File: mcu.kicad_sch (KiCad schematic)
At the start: 11 parts, among them U5 ESP32-S3-WROOM-1

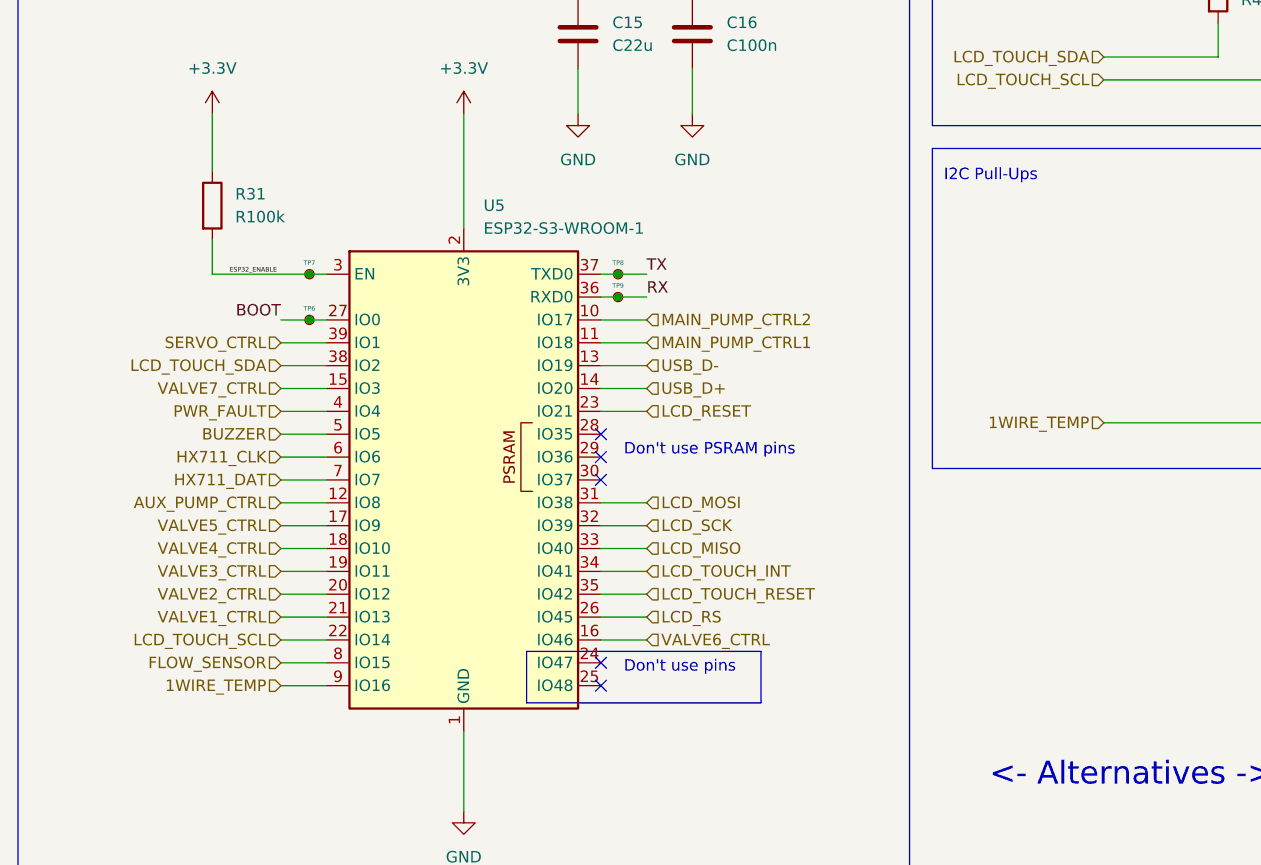
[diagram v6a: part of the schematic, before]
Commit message: Redesign power rails to use barrel jack 12V input
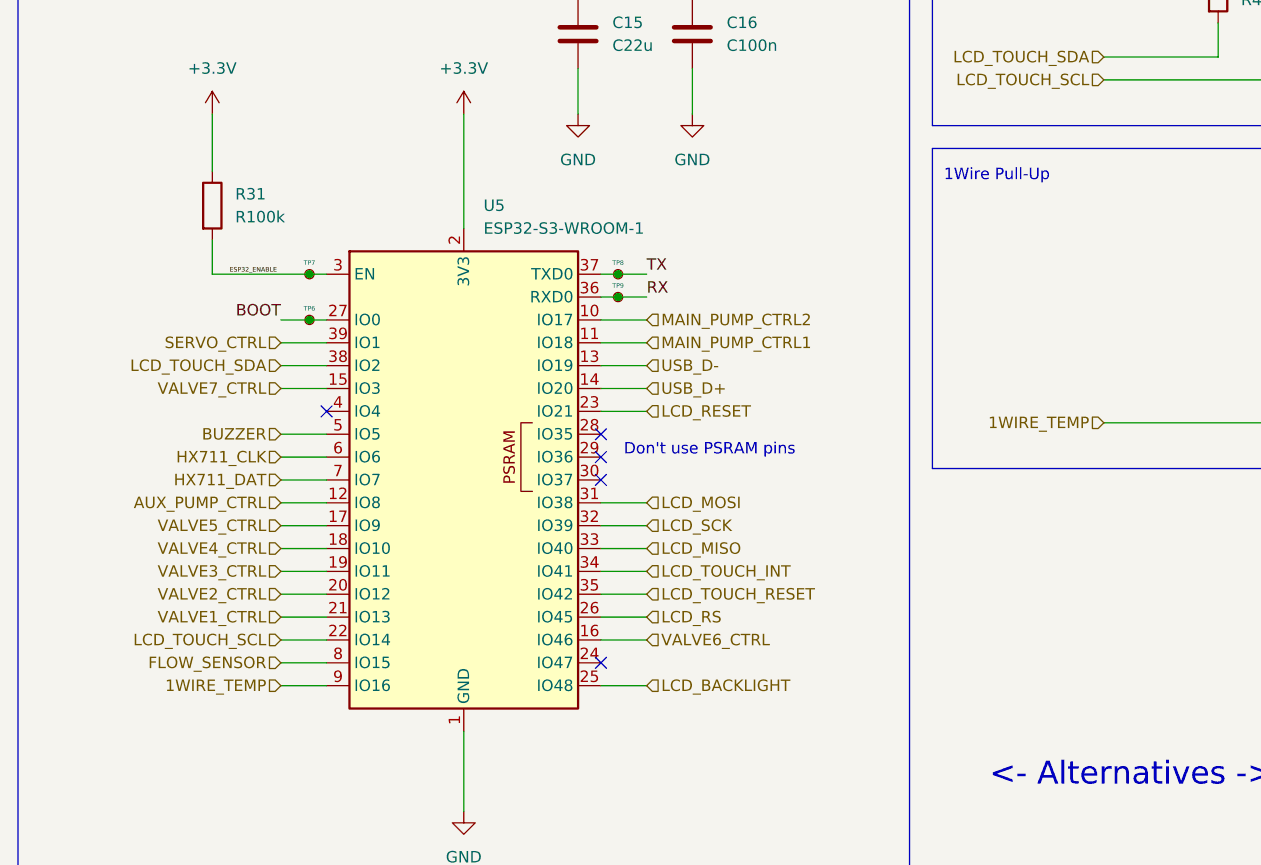
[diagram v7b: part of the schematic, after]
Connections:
- net LCD_BACKLIGHT: now reaches U5.25 (IO48)
- net PWR_FAULT: no longer names the net of U5.4 (IO4)
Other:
- note added: "1Wire Pull-Up"
- note removed: "Don't use pins"
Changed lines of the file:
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@@
   )
   (no_connect (at 78.74 125.73))
-  (no_connect (at 78.74 128.27))
+  (no_connect (at 48.26 97.79))
   (no_connect (at 78.74 105.41))
   (no_connect (at 78.74 102.87))
@@
     (stroke (width 0) (type default))
   )
-  (wire (pts (xy 43.18 97.79) (xy 48.26 97.79))
-    (stroke (width 0) (type default))
-  )
   (wire (pts (xy 43.18 123.19) (xy 48.26 123.19))
     (stroke (width 0) (type default))
@@
     (stroke (width 0) (type default))
   )
+  (wire (pts (xy 83.82 128.27) (xy 78.74 128.27))
+    (stroke (width 0) (type default))
+  )
   (wire (pts (xy 43.18 115.57) (xy 48.26 115.57))
     (stroke (width 0) (type default))
@@
   )
   (rectangle (start 115.57 68.58) (end 168.91 104.14)
-    (stroke (width 0) (type default))
-    (fill (type none))
-  )
-  (rectangle (start 70.485 124.46) (end 96.52 130.175)
     (stroke (width 0) (type default))
     (fill (type none))
@@
     (effects (font (size 2.54 2.54) (thickness 0.508) bold italic (color 255 69 42 1)) (justify left bottom))
   )
-  (text "Don't use pins" (at 81.28 127 0)
-    (effects (font (size 1.27 1.27)) (justify left bottom))
-  )
-  (text "I2C Pull-Ups" (at 116.84 72.39 0)
+  (text "1Wire Pull-Up" (at 116.84 72.39 0)
     (effects (font (size 1.27 1.27)) (justify left bottom))
   )
@@
     (effects (font (size 1.27 1.27)) (justify left))
   )
-  (hierarchical_label "PWR_FAULT" (shape input) (at 43.18 97.79 180) (fields_autoplaced)
-    (effects (font (size 1.27 1.27)) (justify right))
-  )
   (hierarchical_label "1WIRE_TEMP" (shape input) (at 43.18 128.27 180) (fields_autoplaced)
     (effects (font (size 1.27 1.27)) (justify right))
@@
     (effects (font (size 1.27 1.27)) (justify right))
   )
+  (hierarchical_label "LCD_BACKLIGHT" (shape input) (at 83.82 128.27 0) (fields_autoplaced)
+    (effects (font (size 1.27 1.27)) (justify left))
+  )
   (hierarchical_label "LCD_TOUCH_SCL" (shape input) (at 134.62 60.96 180) (fields_autoplaced)

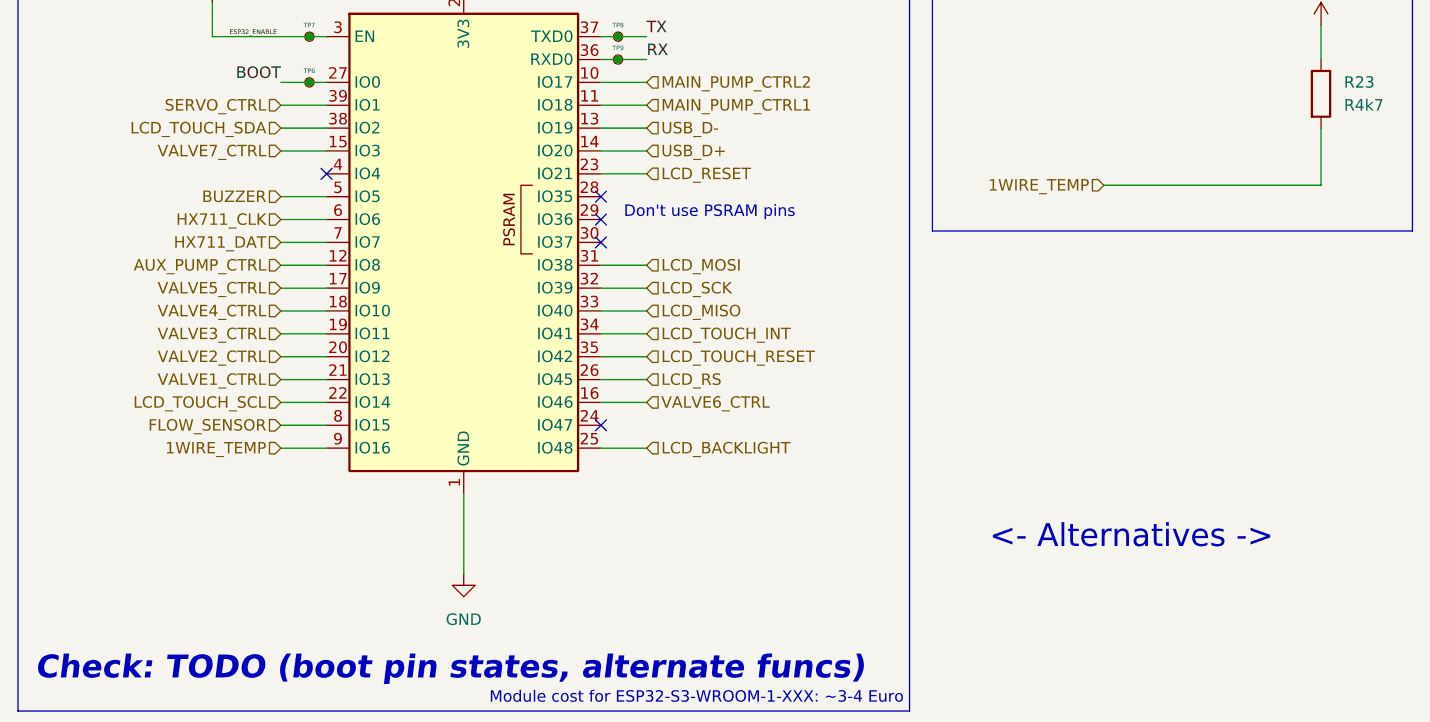
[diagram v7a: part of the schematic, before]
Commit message: Cleanup layout and schematic
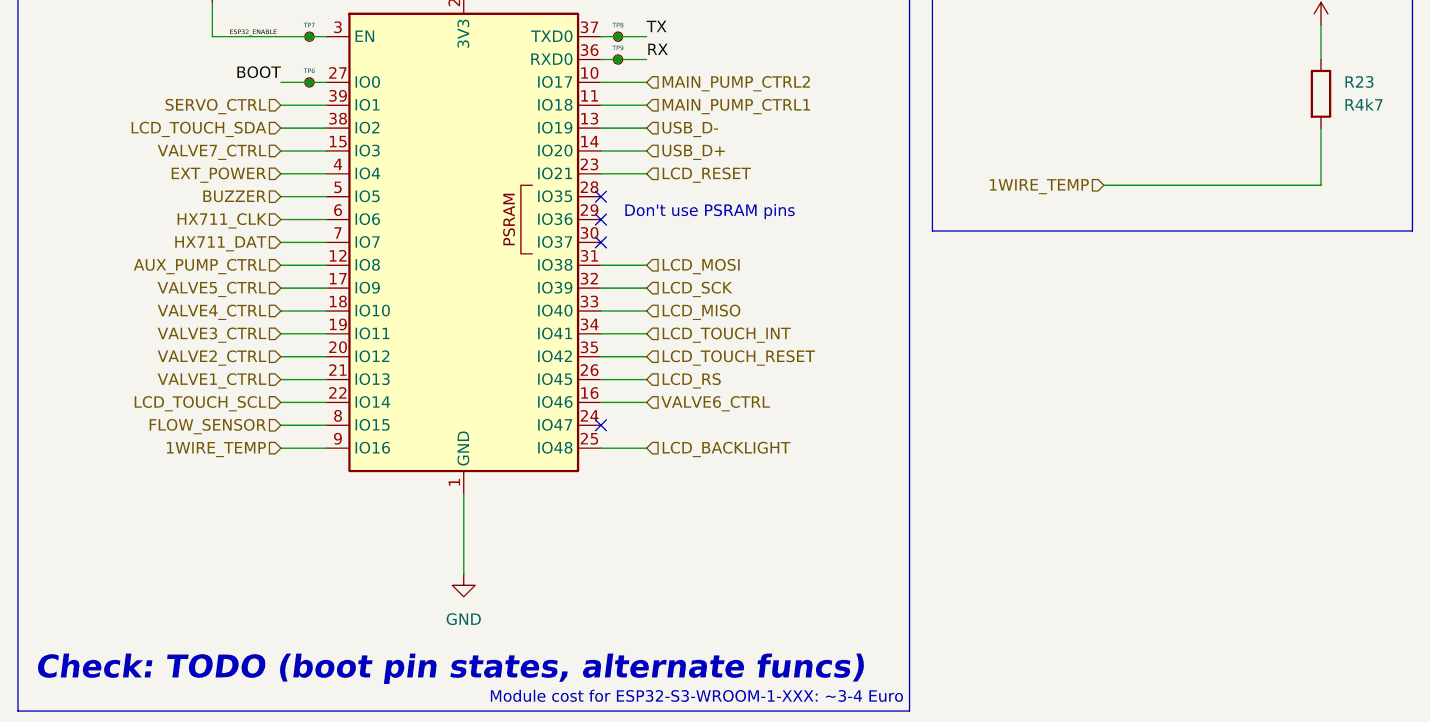
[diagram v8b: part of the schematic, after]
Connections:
- net EXT_POWER: now reaches U5.4 (IO4)
- no-connect marks 5 -> 4
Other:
- note removed: "<- Alternatives ->"
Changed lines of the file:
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@@
   )
   (no_connect (at 78.74 125.73))
-  (no_connect (at 48.26 97.79))
   (no_connect (at 78.74 105.41))
   (no_connect (at 78.74 102.87))
@@
     (stroke (width 0) (type default))
   )
+  (wire (pts (xy 43.18 97.79) (xy 48.26 97.79))
+    (stroke (width 0) (type default))
+  )
   (wire (pts (xy 158.75 81.28) (xy 158.75 85.09))
     (stroke (width 0) (type default))
@@
     (effects (font (size 1.27 1.27)) (justify left bottom))
   )
-  (text "<- Alternatives ->" (at 121.92 139.7 0)
-    (effects (font (size 2.54 2.54)) (justify left bottom))
-  )
   (text "Check: TODO (boot pin states, alternate funcs)" (at 15.875 154.305 0)
     (effects (font (size 2.54 2.54) (thickness 0.508) bold italic (color 255 69 42 1)) (justify left bottom))
@@
     (effects (font (size 1.27 1.27)) (justify right))
   )
+  (hierarchical_label "EXT_POWER" (shape input) (at 43.18 97.79 180) (fields_autoplaced)
+    (effects (font (size 1.27 1.27)) (justify right))
+  )
